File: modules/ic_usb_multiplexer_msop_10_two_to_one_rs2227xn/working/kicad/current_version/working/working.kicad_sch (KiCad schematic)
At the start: 4 parts, among them U1 imsp10mpump21rs2227

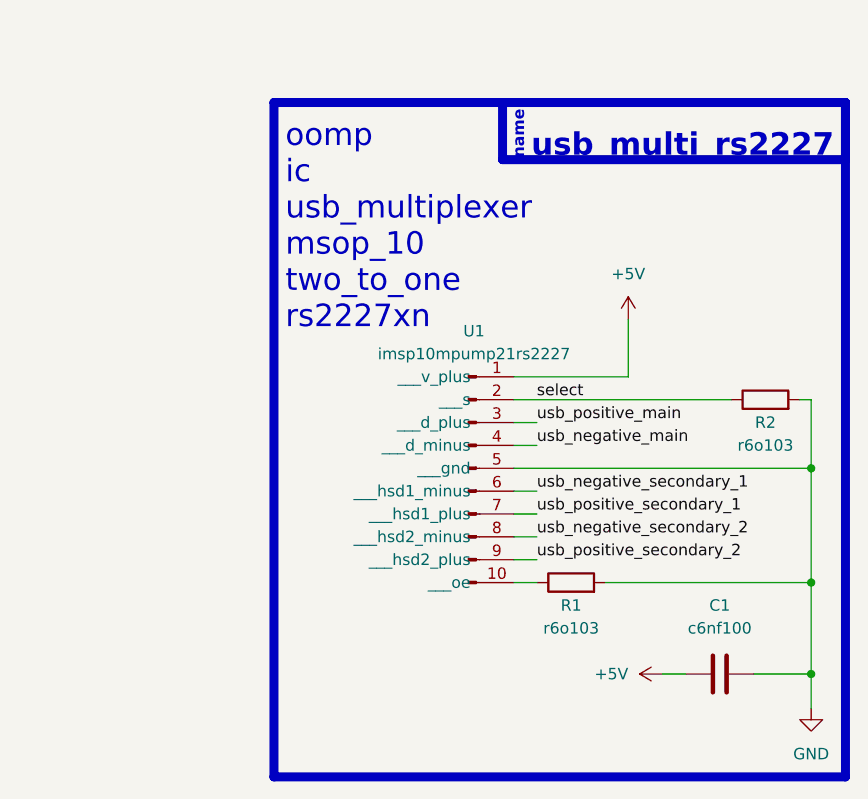
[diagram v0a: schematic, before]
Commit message: fixed formatting to be more consistent
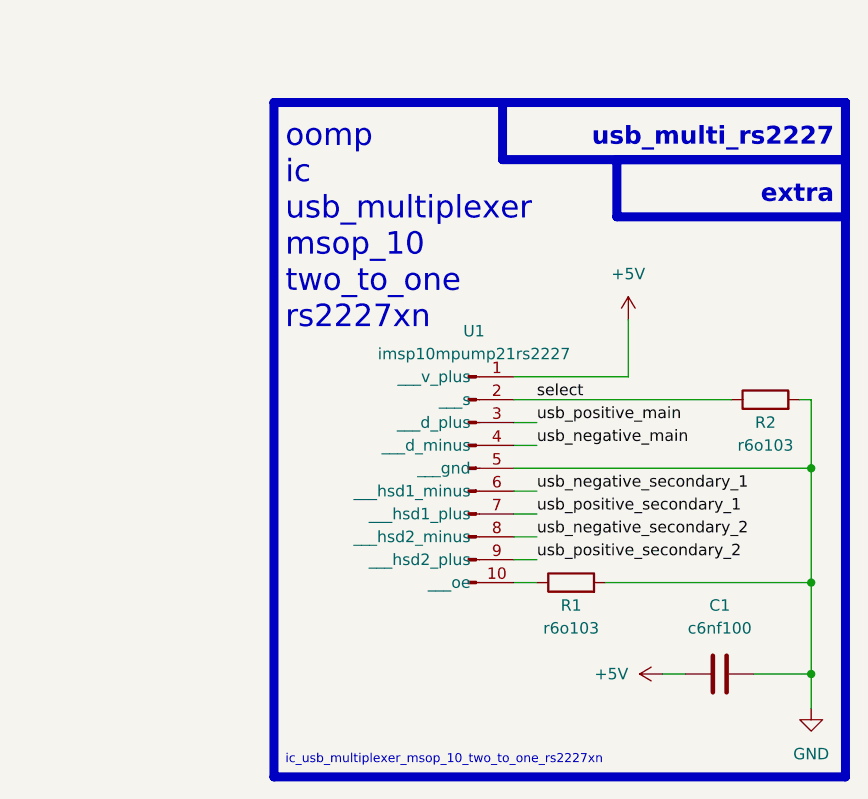
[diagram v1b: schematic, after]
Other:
- note added: "extra"
- note added: "ic_usb_multiplexer_msop_10_two_to_one_rs2227xn"
- note removed: "name"
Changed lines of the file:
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@@
   (rectangle (start 127 39.37) (end 165.1 45.72)
     (stroke (width 1) (type default))
-    (fill (type color) (color 0 0 0 0))
+    (fill (type none))
   )
-  (text "usb_multi_rs2227" (at 163.83 45.72 0)
-    (effects (font (size 2.5 2.5) (thickness 0.8) bold (color 255 255 255 1)) (justify right bottom))
+  (rectangle (start 139.7 45.72) (end 165.1 52.07)
+    (stroke (width 1) (type default))
+    (fill (type none))
   )
-  (text "name" (at 129.54 45.72 90)
-    (effects (font (size 1.27 1.27) (thickness 0.254) bold (color 255 255 255 1)) (justify left bottom))
+  (text "ic_usb_multiplexer_msop_10_two_to_one_rs2227xn" (at 102.87 113.03 0)
+    (effects (font (size 1 1)) (justify left bottom))
+  )
+  (text "usb_multi_rs2227" (at 163.83 44.45 0)
+    (effects (font (size 2 2) (thickness 0.8) bold) (justify right bottom))
   )
   (text "oomp\nic\nusb_multiplexer\nmsop_10\ntwo_to_one\nrs2227xn"
@@
     (effects (font (size 2.5 2.5)) (justify left bottom))
   )
+  (text "extra" (at 163.83 50.8 0)
+    (effects (font (size 2 2) (thickness 0.8) bold) (justify right bottom))
+  )
   (label "usb_negative_secondary_1" (at 130.81 82.55 0) (fields_autoplaced)

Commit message: a few fix ups
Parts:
- renumbered U1 to IC1
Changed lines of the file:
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@@
   (symbol (lib_id "oomlout_oomp_part_symbols:imsp10mpump21rs2227_electronic_ic_msop_10_multiplexer_usb_multiplexer_two_to_one_jiangsu_runic_tech_rs2227xn") (at 123.19 80.01 0) (unit 1)
     (in_bom yes) (on_board yes) (dnp no) (fields_autoplaced)
-    (property "Reference" "U1" (at 123.825 64.77 0)
+    (property "Reference" "IC1" (at 123.825 64.77 0)
       (effects (font (size 1.27 1.27)))
     )
@@
       (project "working"
         (path "/c9993764-076f-44f6-bf4c-6b69ce17c9e4"
-          (reference "U1") (unit 1)
+          (reference "IC1") (unit 1)
         )
       )

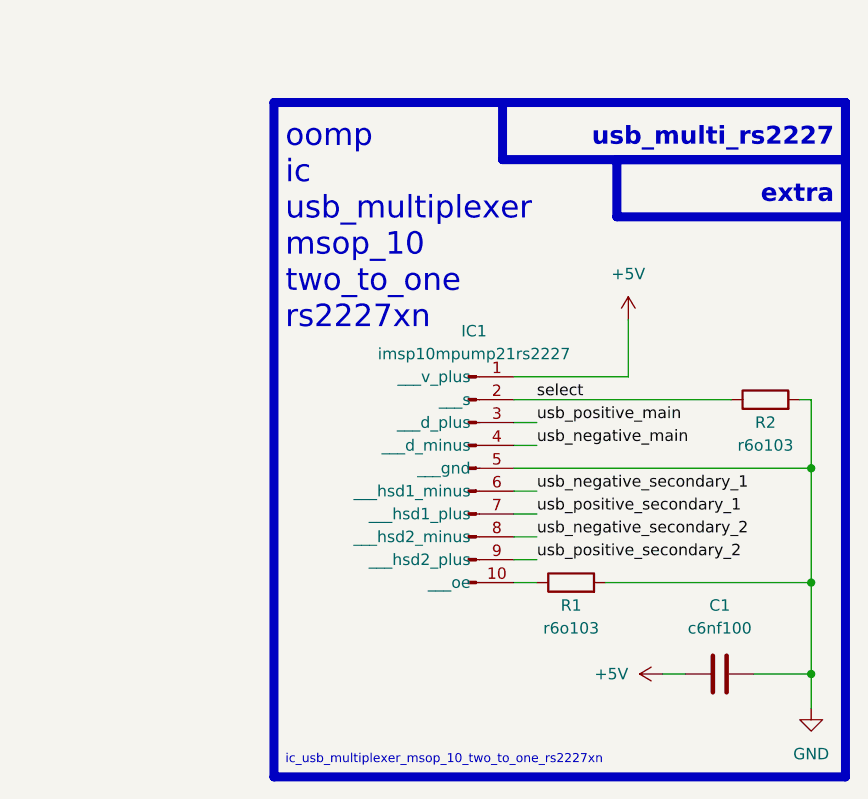
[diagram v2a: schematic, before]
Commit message: schematic formatting
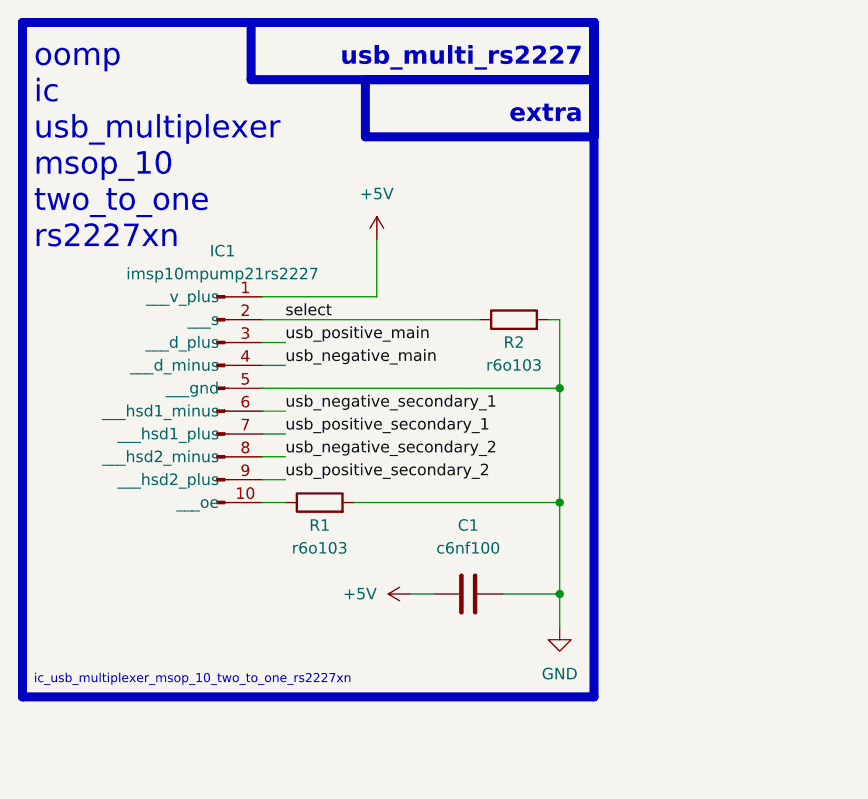
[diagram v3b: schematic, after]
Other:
- moved on the sheet: C1, IC1, R1, R2
